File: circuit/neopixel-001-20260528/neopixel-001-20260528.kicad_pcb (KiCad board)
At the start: 2 copper layers, 114.3 x 114.3 mm, 71 parts, among them J1 Conn_NeoPixel, J2 Conn_01x02_Pin, J3 Conn_01x02_Pin, P1 ESP32C3_{1}, P10 unitV3, P11 unitV4, P12 unitV4, P2 ESP32C3_{1}, P3 ESP32C3_{2}, P4 ESP32C3_{2}, P5 unitV1, P6 unitV1, P7 unitV2, P8 unitV2, P9 unitV3, Q1 NMOS, Q2 NMOS, Q3 NMOS, SW1 SW_SPST_LED, SW2 SW_SPST_LED, SW4 SW_SPST_LED, U1 SSD1306, U2 Aexit_0-50_Voltmeter, U3 74AHC1G04, U4 74AHC1G04, U5 74AHC1G04

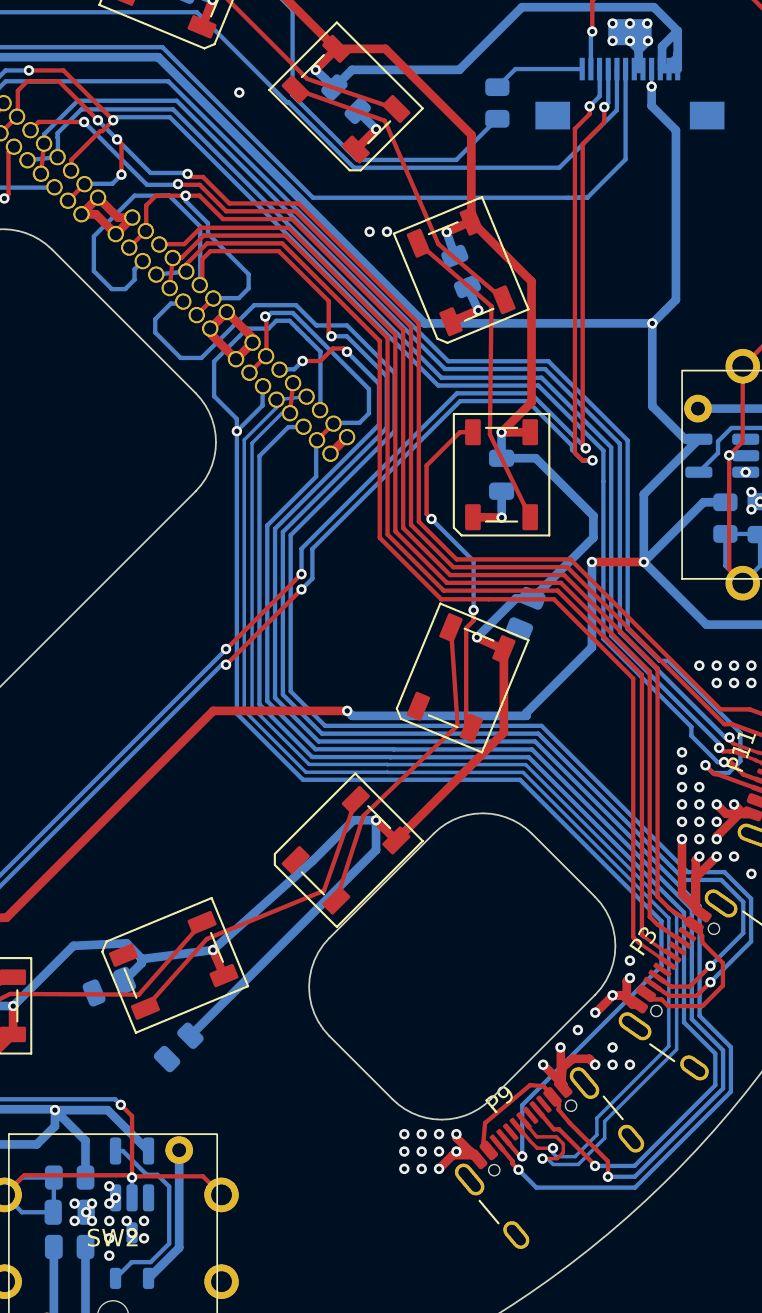
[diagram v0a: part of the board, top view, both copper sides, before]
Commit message: Update ラインセンサ基板を進めた、GND孤立がひどい
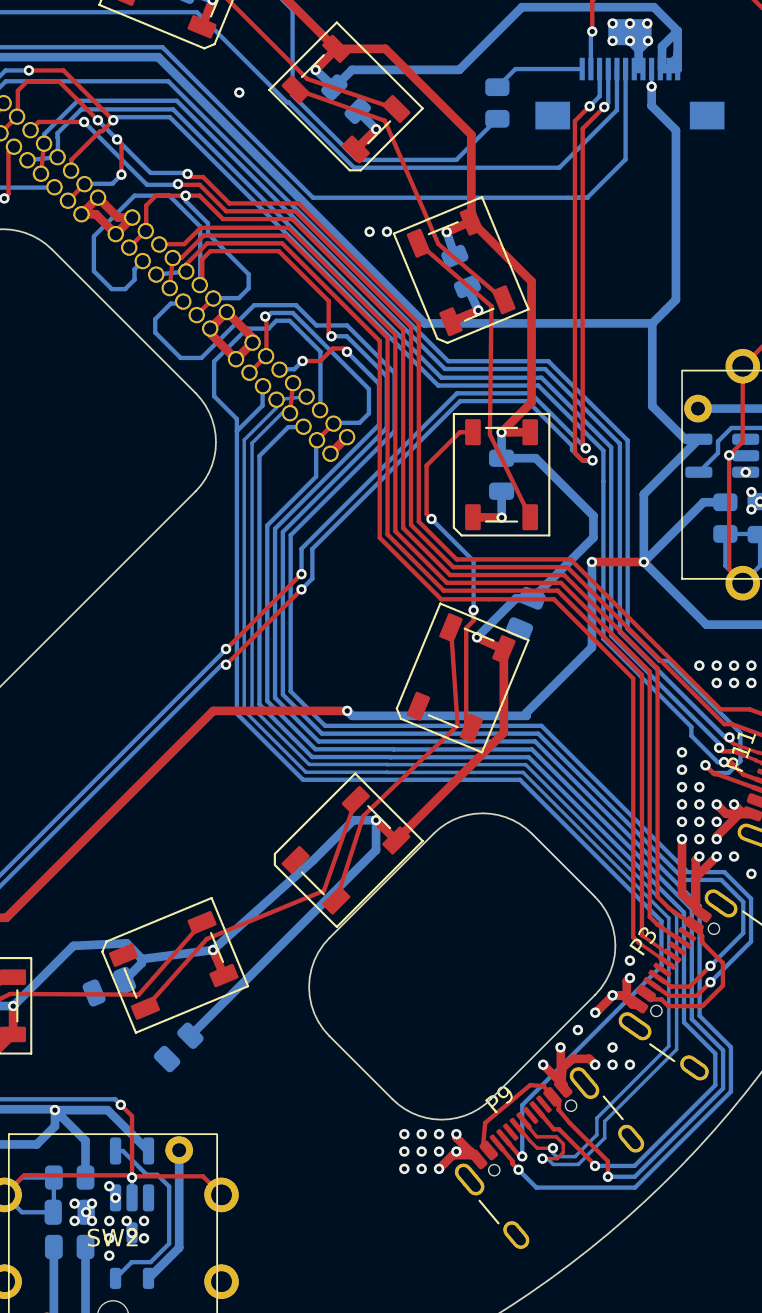
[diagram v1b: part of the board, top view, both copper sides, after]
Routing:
- net P5_CC: vias 2 -> 1
- net GND: vias 175 -> 174
- net +3.3V: vias 11 -> 10

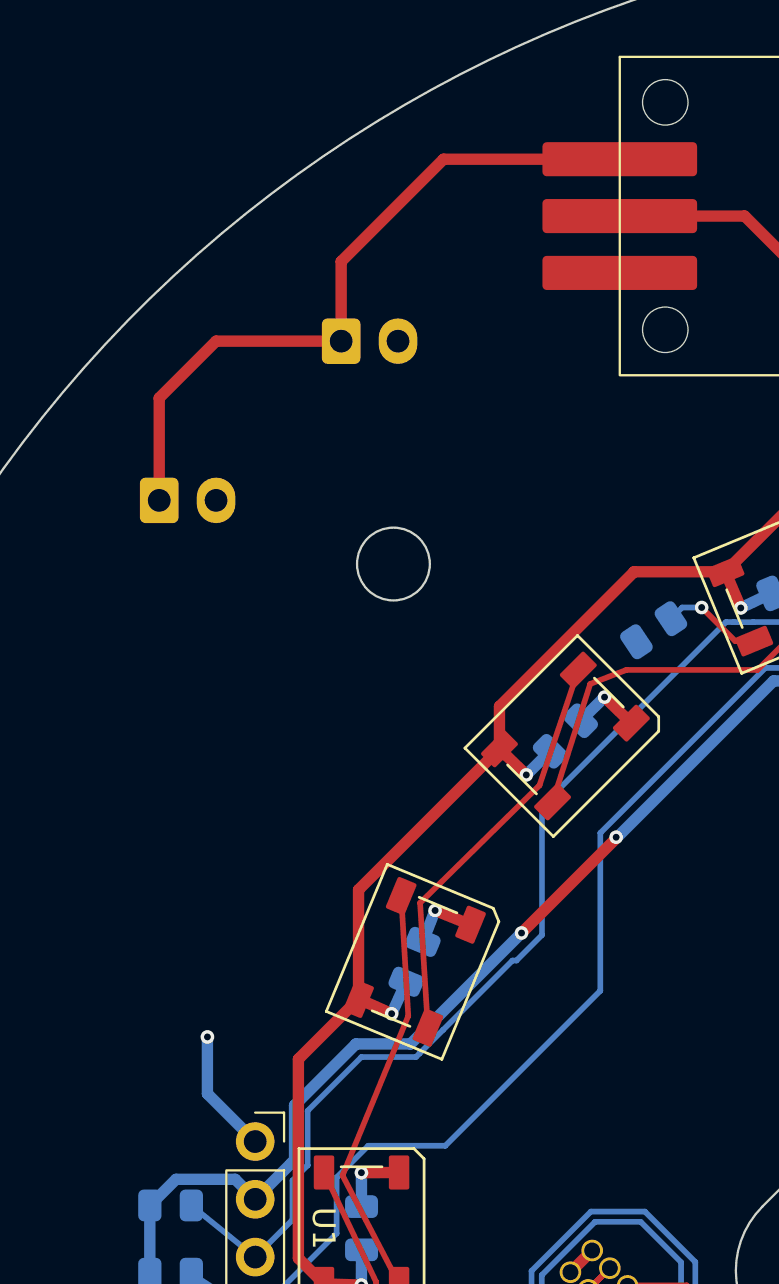
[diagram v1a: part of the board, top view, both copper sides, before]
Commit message: Update ネオピクセル基板の+48Vラインの配線幅を2mmにした
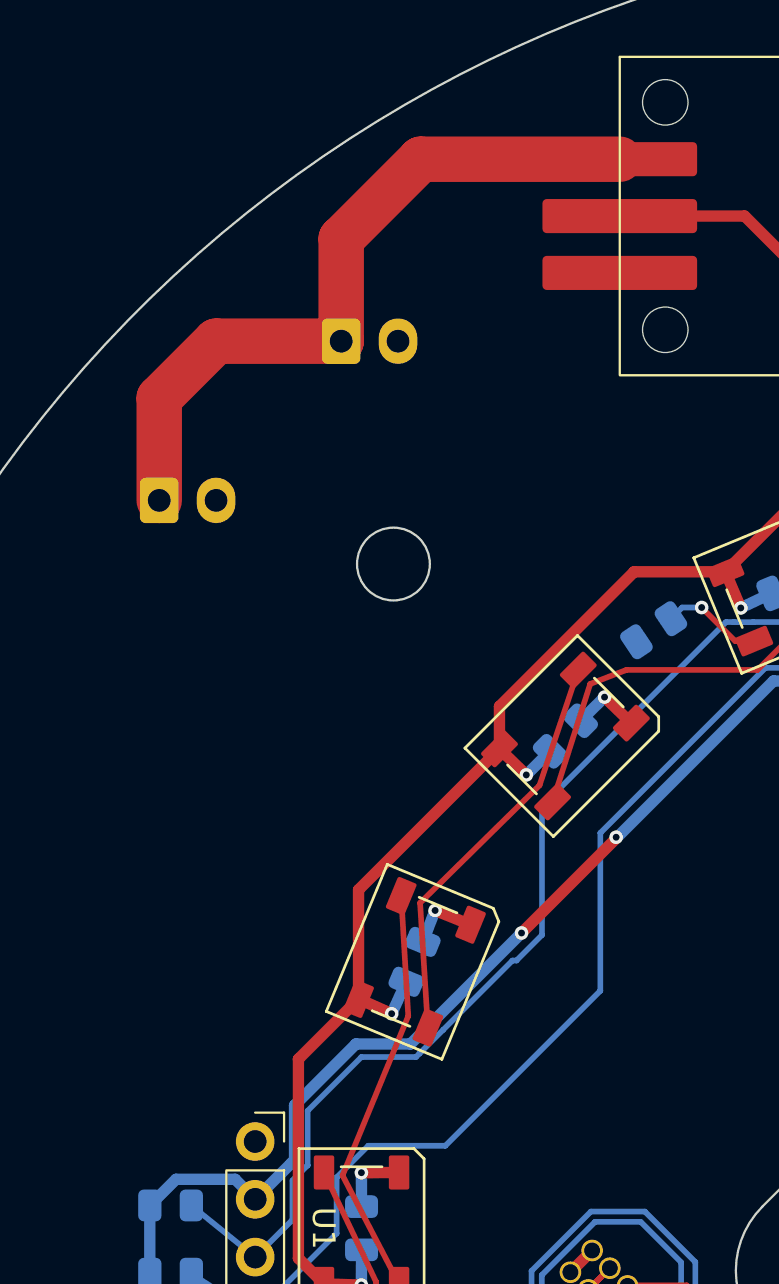
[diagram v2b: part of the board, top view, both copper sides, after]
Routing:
- net GND: track 189.3 -> 183.8 mm, vias 174 -> 173
- net +48V: track 31.1 -> 31.7 mm

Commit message: Update ネオピクセル基板のビア打ち終わった
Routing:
- net GND: vias 173 -> 5133

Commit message: Update ネオピクセル基板のシルクスクリーンを整えた
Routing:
- net GND: vias 5133 -> 4966
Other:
- board text added: "NeoPixel-001"

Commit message: Update NeoPixel基板をプッシュした
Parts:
- J1: value Conn_NeoPixel -> Conn_Sub
- P10, P9: value unitV3 -> UnitV3
- P11, P12: value unitV4 -> UnitV4
- P5, P6: value unitV1 -> UnitV1
- P7, P8: value unitV2 -> UnitV2
- Q1, Q2, Q3: value NMOS -> BSS138
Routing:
- net GND: vias 4966 -> 4867
- net +3.3V: vias 10 -> 6
